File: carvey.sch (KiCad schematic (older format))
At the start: 2 parts, among them J1 Conn_01x04, SW1 SW_Push_Dual

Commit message: Track too near pad
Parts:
- SW1: symbol SW_Push_Dual -> SW_Push_Dual-RESCUE-carvey
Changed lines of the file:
@@
 EESchema Schematic File Version 3
+LIBS:carvey-rescue
 LIBS:power
 LIBS:device
@@
 	3485 3355 3490 3355
 $Comp
-L SW_Push_Dual SW1
+L SW_Push_Dual-RESCUE-carvey SW1
 U 1 1 5ADDB325
 P 3285 3235

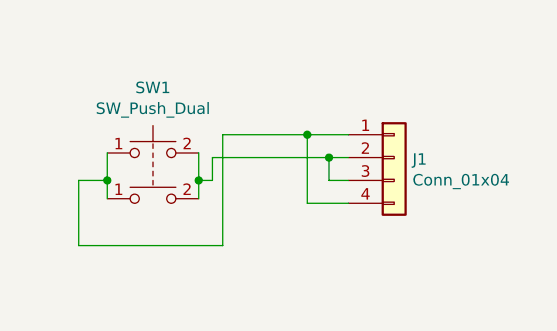
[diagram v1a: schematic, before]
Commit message: Add new board outline with external overhang for alligator clips, need to add the pads
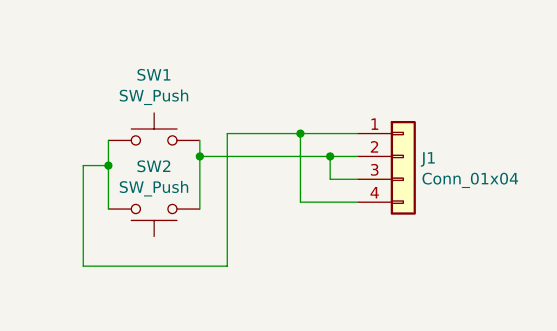
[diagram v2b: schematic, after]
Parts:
- removed SW1: SW_Push_Dual, KiCad/Buttons_Switches_SMD.pretty:SW_SPST_B3S-1000, symbol SW_Push_Dual-RESCUE-carvey
- added SW1, SW2: SW_Push, KiCad/Buttons_Switches_SMD.pretty:SW_SPST_B3U-1000P, symbol SW_Push
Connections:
- wire segments 16 -> 12
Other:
- moved on the sheet: J1
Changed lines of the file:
@@
 L Conn_01x04 J1
 U 1 1 5ADC7CA7
-P 4340 3255
-F 0 "J1" H 4420 3247 50  0000 L CNN
-F 1 "Conn_01x04" H 4420 3156 50  0000 L CNN
-F 2 "KiCad/Connectors_JST.pretty:JST_PH_S4B-PH-SM4-TB_04x2.00mm_Angled" H 4340 3255 50  0001 C CNN
-F 3 "" H 4340 3255 50  0001 C CNN
-	1    4340 3255
+P 4380 3250
+F 0 "J1" H 4460 3242 50  0000 L CNN
+F 1 "Conn_01x04" H 4460 3151 50  0000 L CNN
+F 2 "KiCad/Connectors_JST.pretty:JST_PH_S4B-PH-SM4-TB_04x2.00mm_Angled" H 4380 3250 50  0001 C CNN
+F 3 "" H 4380 3250 50  0001 C CNN
+	1    4380 3250
 	1    0    0    -1
 $EndComp
-Connection ~ 3485 3355
-Wire Wire Line
-	3590 3155 3590 3640
-Wire Wire Line
-	3590 3640 2960 3640
-Wire Wire Line
-	2960 3640 2960 3355
-Wire Wire Line
-	2960 3355 3085 3355
-Connection ~ 3085 3355
-Wire Wire Line
-	4140 3155 3590 3155
-Wire Wire Line
-	4140 3255 3545 3255
-Wire Wire Line
-	3545 3255 3545 3355
-Wire Wire Line
-	3545 3355 3480 3355
-Wire Wire Line
-	4140 3355 4055 3355
-Wire Wire Line
-	4055 3355 4055 3255
-Connection ~ 4055 3255
-Wire Wire Line
-	4140 3455 3960 3455
-Wire Wire Line
-	3960 3455 3960 3155
-Connection ~ 3960 3155
-Wire Wire Line
-	3085 3355 3085 3235
-Wire Wire Line
-	3085 3435 3085 3350
-Wire Wire Line
-	3485 3235 3485 3435
-Wire Wire Line
-	3485 3355 3490 3355
 $Comp
-L SW_Push_Dual-RESCUE-carvey SW1
-U 1 1 5ADDB325
-P 3285 3235
-F 0 "SW1" H 3285 3520 50  0000 C CNN
-F 1 "SW_Push_Dual" H 3285 3429 50  0000 C CNN
-F 2 "KiCad/Buttons_Switches_SMD.pretty:SW_SPST_B3S-1000" H 3285 3435 50  0001 C CNN
-F 3 "" H 3285 3435 50  0001 C CNN
-	1    3285 3235
+L SW_Push SW1
+U 1 1 5AFD3A54
+P 3290 3180
+F 0 "SW1" H 3290 3465 50  0000 C CNN
+F 1 "SW_Push" H 3290 3374 50  0000 C CNN
+F 2 "KiCad/Buttons_Switches_SMD.pretty:SW_SPST_B3U-1000P" H 3290 3380 50  0001 C CNN
+F 3 "" H 3290 3380 50  0001 C CNN
+	1    3290 3180
 	1    0    0    -1
 $EndComp
+$Comp
+L SW_Push SW2
+U 1 1 5AFD3A92
+P 3290 3480
+F 0 "SW2" H 3290 3295 50  0000 C CNN
+F 1 "SW_Push" H 3290 3386 50  0000 C CNN
+F 2 "KiCad/Buttons_Switches_SMD.pretty:SW_SPST_B3U-1000P" H 3290 3680 50  0001 C CNN
+F 3 "" H 3290 3680 50  0001 C CNN
+	1    3290 3480
+	-1   0    0    1
+$EndComp
+Wire Wire Line
+	3090 3180 3090 3480
+Wire Wire Line
+	3490 3180 3490 3480
+Wire Wire Line
+	4180 3250 3490 3250
+Connection ~ 3490 3250
+Wire Wire Line
+	4180 3350 4060 3350
+Wire Wire Line
+	4060 3350 4060 3250
+Connection ~ 4060 3250
+Wire Wire Line
+	4180 3150 3610 3150
+Wire Wire Line
+	3610 3150 3610 3730
+Wire Wire Line
+	3610 3730 2980 3730
+Wire Wire Line
+	2980 3730 2980 3290
+Wire Wire Line
+	2980 3290 3090 3290
+Connection ~ 3090 3290
+Wire Wire Line
+	4180 3450 3930 3450
+Wire Wire Line
+	3930 3450 3930 3150
+Connection ~ 3930 3150
 $EndSCHEMATC

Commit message: New version of the board with protruding pads for the alligator clips
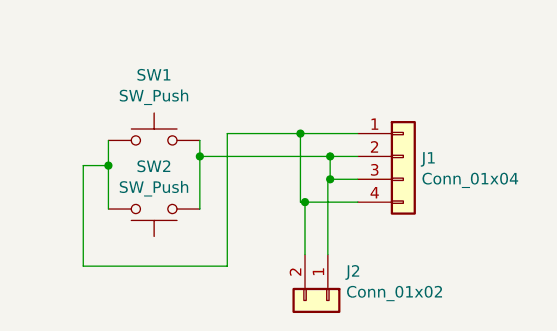
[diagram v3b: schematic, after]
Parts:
- added J2: Conn_01x02, alligator_pads:TouchSlider-2_10x7mm, symbol Conn_01x02
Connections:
- net at J1.1 (Pin_1), J1.4 (Pin_4), SW1.1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: now also J2.2 (Pin_2)
- net at J1.2 (Pin_2), J1.3 (Pin_3), SW1.2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: now also J2.1 (Pin_1)
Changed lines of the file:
@@
 	-1   0    0    1
+$EndComp
+$Comp
+L Conn_01x02 J2
+U 1 1 5AFD5A49
+P 4050 3880
+F 0 "J2" V 3923 3960 50  0000 L CNN
+F 1 "Conn_01x02" V 4014 3960 50  0000 L CNN
+F 2 "alligator_pads:TouchSlider-2_10x7mm" H 4050 3880 50  0001 C CNN
+F 3 "" H 4050 3880 50  0001 C CNN
+	1    4050 3880
+	0    1    1    0
 $EndComp
 Wire Wire Line
@@
 Connection ~ 3490 3250
 Wire Wire Line
-	4180 3350 4060 3350
+	4050 3350 4180 3350
 Wire Wire Line
 	4060 3350 4060 3250
@@
 	3930 3450 3930 3150
 Connection ~ 3930 3150
+Wire Wire Line
+	3950 3680 3950 3450
+Connection ~ 3950 3450
+Wire Wire Line
+	4050 3680 4050 3350
+Connection ~ 4060 3350
 $EndSCHEMATC
